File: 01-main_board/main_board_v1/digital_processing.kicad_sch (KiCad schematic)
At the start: 34 parts, among them IC9 LSF0108PWR, T1 749013011

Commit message: altered ethernet layout
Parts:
- R15, R16, R17, R18, R19, R26, R29, R30, R31, R32, R34, R4: footprint (none) -> Resistor_SMD:R_0402_1005Metric
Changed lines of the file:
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@@
 			)
 		)
-		(property "Footprint" ""
+		(property "Footprint" "Resistor_SMD:R_0402_1005Metric"
 			(at 167.64 91.44 0)
 			(effects
@@
 			)
 		)
-		(property "Footprint" ""
+		(property "Footprint" "Resistor_SMD:R_0402_1005Metric"
 			(at 210.82 52.07 0)
 			(effects
@@
 			)
 		)
-		(property "Footprint" ""
+		(property "Footprint" "Resistor_SMD:R_0402_1005Metric"
 			(at 132.08 83.82 0)
 			(effects
@@
 			)
 		)
-		(property "Footprint" ""
+		(property "Footprint" "Resistor_SMD:R_0402_1005Metric"
 			(at 207.01 38.1 0)
 			(effects
@@
 			)
 		)
-		(property "Footprint" ""
+		(property "Footprint" "Resistor_SMD:R_0402_1005Metric"
 			(at 210.82 87.63 0)
 			(effects
@@
 			)
 		)
-		(property "Footprint" ""
+		(property "Footprint" "Resistor_SMD:R_0402_1005Metric"
 			(at 171.45 87.63 0)
 			(effects
@@
 			)
 		)
-		(property "Footprint" ""
+		(property "Footprint" "Resistor_SMD:R_0402_1005Metric"
 			(at 210.82 69.85 0)
 			(effects
@@
 			)
 		)
-		(property "Footprint" ""
+		(property "Footprint" "Resistor_SMD:R_0402_1005Metric"
 			(at 210.82 34.29 0)
 			(effects
@@
 			)
 		)
-		(property "Footprint" ""
+		(property "Footprint" "Resistor_SMD:R_0402_1005Metric"
 			(at 128.27 80.01 0)
 			(effects
@@
 			)
 		)
-		(property "Footprint" ""
+		(property "Footprint" "Resistor_SMD:R_0402_1005Metric"
 			(at 207.01 73.66 0)
 			(effects
@@
 			)
 		)
-		(property "Footprint" ""
+		(property "Footprint" "Resistor_SMD:R_0402_1005Metric"
 			(at 207.01 91.44 0)
 			(effects
@@
 			)
 		)
-		(property "Footprint" ""
+		(property "Footprint" "Resistor_SMD:R_0402_1005Metric"
 			(at 207.01 55.88 0)
 			(effects

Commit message: finished analog input traces
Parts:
- IC9: footprint QFN50P450X250X100-21N-D -> 22XT_Main:SOP65P640X120-20N
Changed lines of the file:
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@@
 			)
 		)
-		(property "Footprint" "QFN50P450X250X100-21N-D"
+		(property "Footprint" "22XT_Main:SOP65P640X120-20N"
 			(at 39.7 68.58 0)
 			(effects

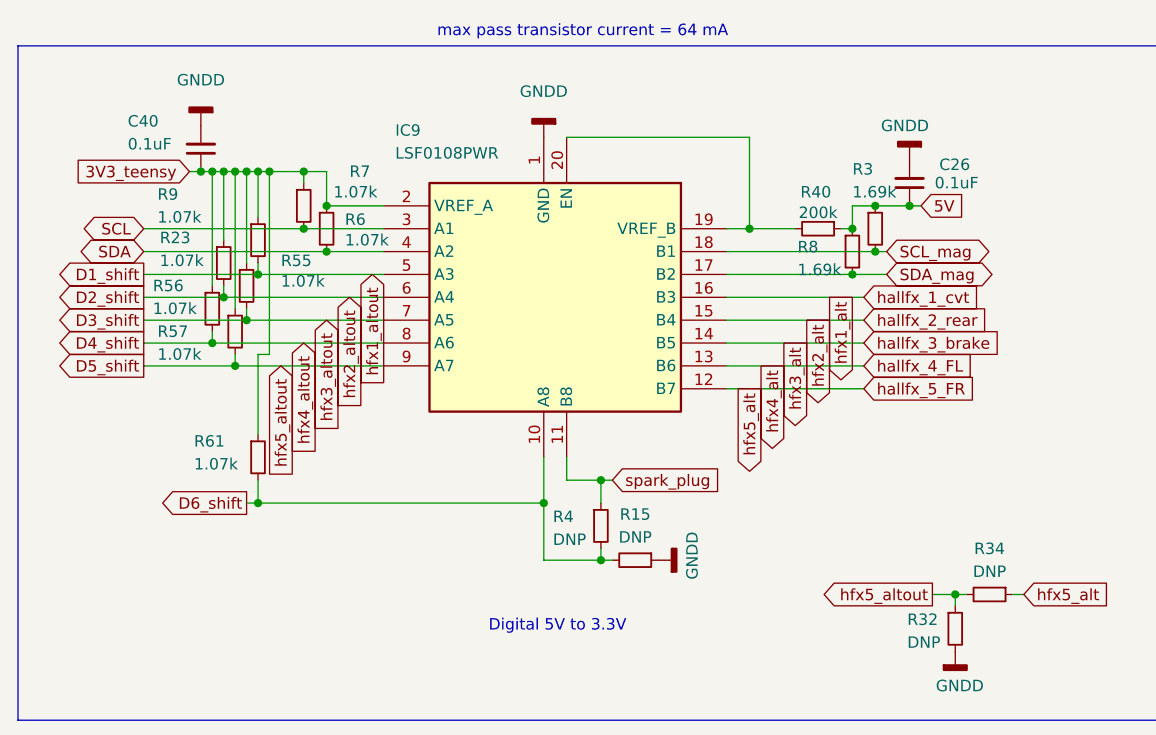
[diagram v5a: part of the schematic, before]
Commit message: attempted to fix gnd plane, updated vias
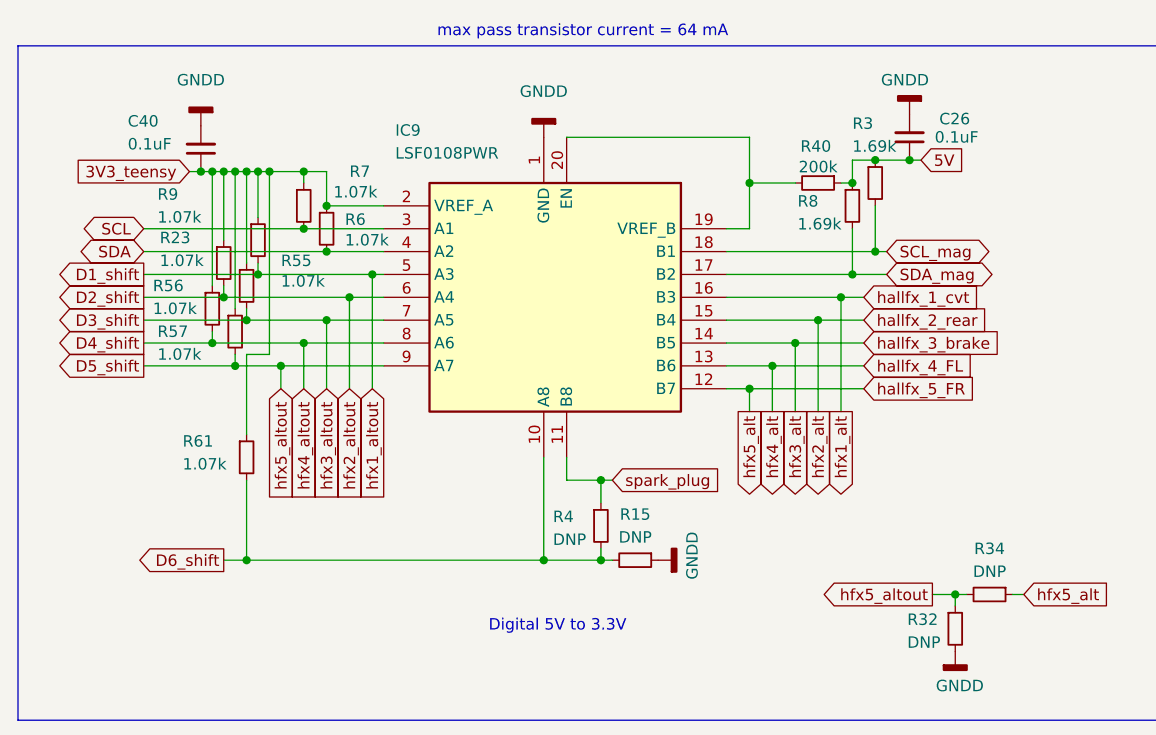
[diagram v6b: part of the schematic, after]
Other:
- moved on the sheet: C26, R3, R40, R61, R8

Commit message: Added main board footprint library
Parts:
- D2: footprint SOT95P280X145-5N -> (none)
- T1: footprint 749013011 -> (none)
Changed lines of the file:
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@@
 			)
 		)
-		(property "Footprint" "749013011"
+		(property "Footprint" ""
 			(at 146.05 223.19 0)
 			(effects
@@
 			)
 		)
-		(property "Footprint" "SOT95P280X145-5N"
+		(property "Footprint" ""
 			(at 215.9 229.54 0)
 			(effects

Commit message: Re-assigned all footprints
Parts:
- D2: footprint (none) -> Package_TO_SOT_SMD:SOT-23-5
- T1: footprint (none) -> 22XT_Main:749013011
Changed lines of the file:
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@@
 			)
 		)
-		(property "Footprint" ""
+		(property "Footprint" "22XT_Main:749013011"
 			(at 146.05 223.19 0)
 			(effects
@@
 			)
 		)
-		(property "Footprint" ""
+		(property "Footprint" "Package_TO_SOT_SMD:SOT-23-5"
 			(at 215.9 229.54 0)
 			(effects
